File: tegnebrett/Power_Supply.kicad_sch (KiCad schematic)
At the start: 45 parts, among them J9 PJ-002A, U7 TPS54294PWP2, U8 TPS54294PWP1

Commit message: fix: fix footprint paths for symbols
After moving the footprints around, some symbols were without
footprints.
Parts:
- J9: footprint CUI_PJ-002A -> tegnebrett_modules:CUI_PJ-002A
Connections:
- net POWER_IN: now also C69.1, C71.1, C80.1, C82.1, J9.3, U7.1 (VIN1), U7.16 (VIN2), U7.5 (EN1)
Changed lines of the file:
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@@
-	)
-	(junction
-		(at 92.71 27.94)
-		(diameter 0)
-		(color 0 0 0 0)
 	)
 	(junction
@@
 	(wire
 		(pts
-			(xy 83.82 27.94) (xy 92.71 27.94)
-		)
-		(stroke
-			(width 0)
-			(type default)
-		)
-	)
-	(wire
-		(pts
 			(xy 166.37 52.07) (xy 168.91 52.07)
 		)
@@
 	(wire
 		(pts
-			(xy 92.71 27.94) (xy 102.87 27.94)
+			(xy 83.82 27.94) (xy 102.87 27.94)
 		)
 		(stroke
@@
 			(width 0)
 			(type default)
+		)
+	)
+	(global_label "POWER_IN"
+		(shape input)
+		(at 96.52 27.94 90)
+		(fields_autoplaced yes)
+		(effects
+			(font
+				(size 1.27 1.27)
+			)
+			(justify left)
+		)
+		(property "Intersheetrefs" "${INTERSHEET_REFS}"
+			(at 96.52 15.581 90)
+			(effects
+				(font
+					(size 1.27 1.27)
+				)
+				(justify left)
+				(hide yes)
+			)
 		)
 	)
@@
 	)
 	(symbol
-		(lib_id "power:PWR_FLAG")
-		(at 92.71 27.94 0)
-		(unit 1)
-		(exclude_from_sim no)
-		(in_bom yes)
-		(on_board yes)
-		(dnp no)
-		(property "Reference" "#FLG03"
-			(at 92.71 26.035 0)
-			(effects
-				(font
-					(size 1.27 1.27)
-				)
-				(hide yes)
-			)
-		)
-		(property "Value" "PWR_FLAG"
-			(at 97.79 29.21 0)
-			(effects
-				(font
-					(size 1.27 1.27)
-				)
-			)
-		)
-		(property "Footprint" ""
-			(at 92.71 27.94 0)
-			(effects
-				(font
-					(size 1.27 1.27)
-				)
-				(hide yes)
-			)
-		)
-		(property "Datasheet" "~"
-			(at 92.71 27.94 0)
-			(effects
-				(font
-					(size 1.27 1.27)
-				)
-				(hide yes)
-			)
-		)
-		(property "Description" "Special symbol for telling ERC where power comes from"
-			(at 92.71 27.94 0)
-			(effects
-				(font
-					(size 1.27 1.27)
-				)
-				(hide yes)
-			)
-		)
-		(pin "1"
-		)
-		(instances
-			(project "getting-started"
-				(path "/d9a31669-c5f1-42a7-9461-3df04b9a4e62/2b77afb8-d96a-4ff9-98fc-590ed1d53f5b"
-					(reference "#FLG03")
-					(unit 1)
-				)
-			)
-		)
-	)
-	(symbol
 		(lib_id "Device:L")
 		(at 88.9 54.61 90)
@@
 			)
 		)
-		(property "Footprint" "CUI_PJ-002A"
+		(property "Footprint" "tegnebrett_modules:CUI_PJ-002A"
 			(at 78.74 27.94 0)
 			(effects

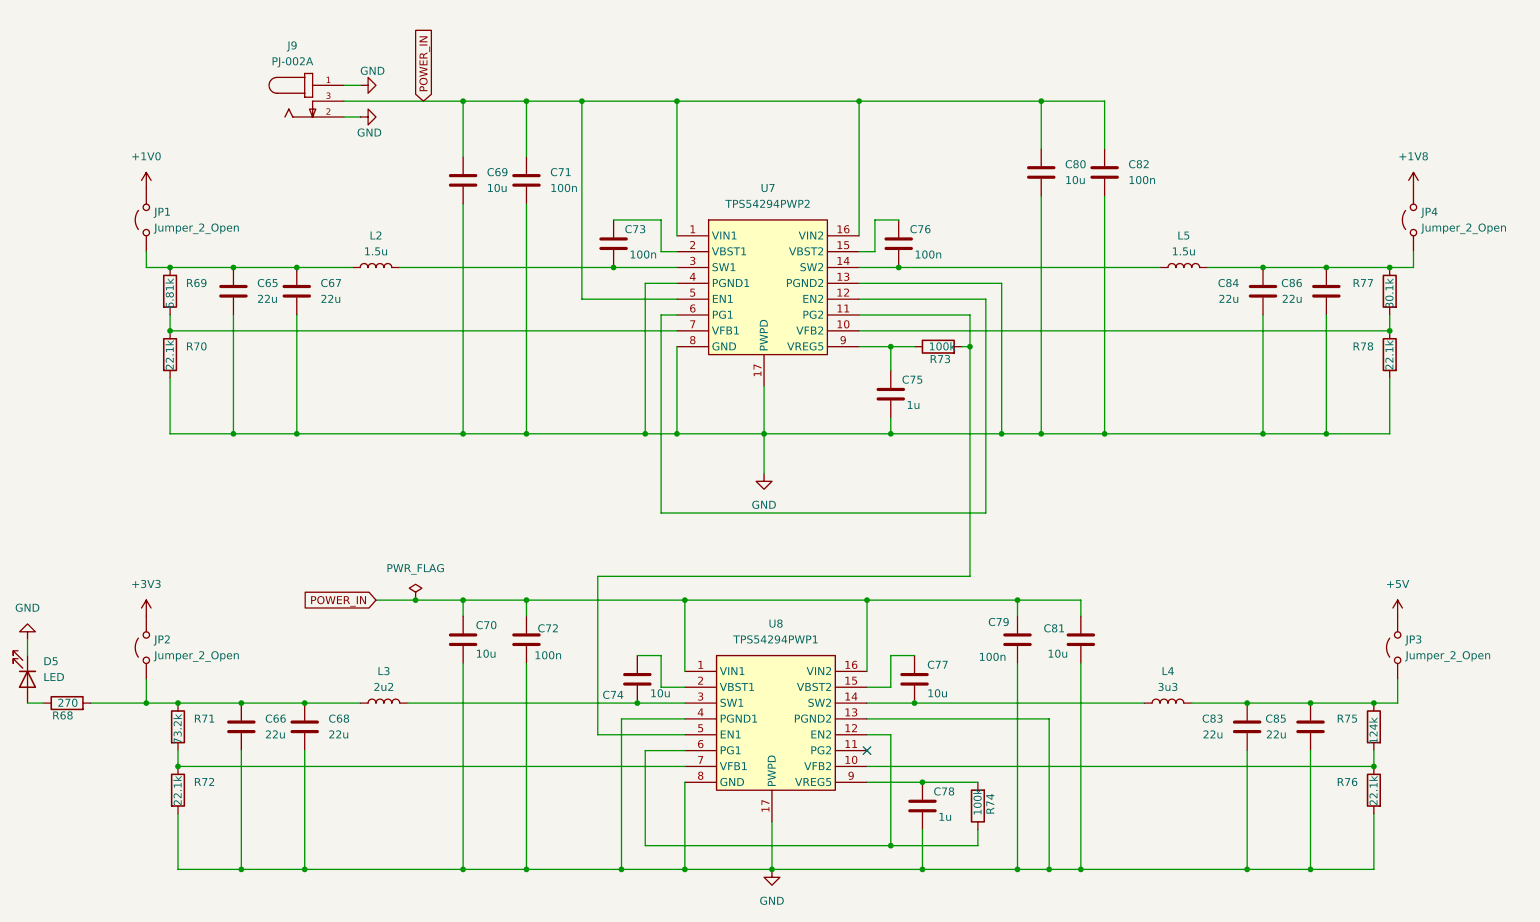
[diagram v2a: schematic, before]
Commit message: fix: add PWR_FLAG symbol to Power supply schematic
This reduces errors, now we only have one error left.
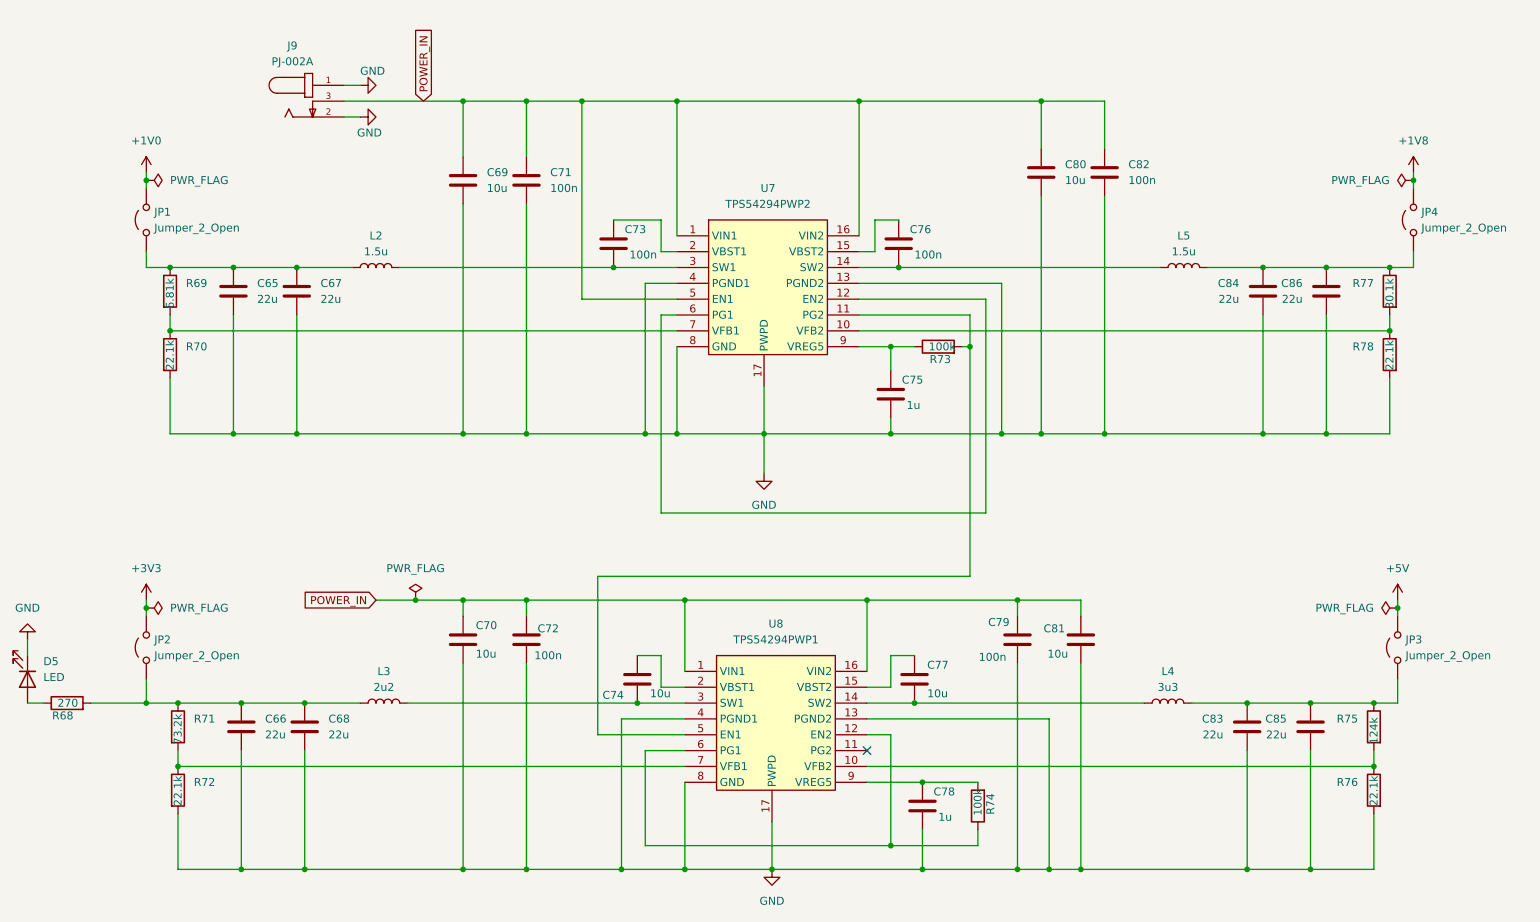
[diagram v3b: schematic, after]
